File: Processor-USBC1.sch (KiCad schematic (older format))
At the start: 8 parts, among them J16 201267-0005, Q13 BSS138W, U28 PESD5V0X1BQ,115

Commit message: PVT
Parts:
- renumbered C104 to C99, Q13 to Q14, R77 to R68, R78 to R69, R79 to R70, R80 to R71, U28 to U26
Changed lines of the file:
@@
 encoding utf-8
 Sheet 11 24
-Title "Phoenix DVT"
-Date "2020-05-18"
+Title "Phoenix PVT"
+Date "2020-07-19"
 Rev "1"
 Comp ""
@@
 	7800 3500 7800 3400
 $Comp
-L supply-alias:GND #PWR0235
+L supply-alias:GND #PWR0223
 U 1 1 5E9C1E1F
 P 4600 2500
-F 0 "#PWR0235" H 4600 2250 50  0001 C CNN
+F 0 "#PWR0223" H 4600 2250 50  0001 C CNN
 F 1 "GND" H 4600 2350 50  0000 C CNN
 F 2 "" H 4600 2500 50  0001 C CNN
@@
 	6900 2900 6900 4100
 $Comp
-L supply-alias:GND #PWR0240
+L supply-alias:GND #PWR0228
 U 1 1 5EBF6DC2
 P 6900 4400
-F 0 "#PWR0240" H 6900 4150 50  0001 C CNN
+F 0 "#PWR0228" H 6900 4150 50  0001 C CNN
 F 1 "GND" H 6900 4250 50  0000 C CNN
 F 2 "" H 6900 4400 50  0001 C CNN
@@
 	6900 4400 6900 4300
 $Comp
-L supply-alias:GND #PWR0241
+L supply-alias:GND #PWR0229
 U 1 1 5E9C1E2B
 P 7100 4400
-F 0 "#PWR0241" H 7100 4150 50  0001 C CNN
+F 0 "#PWR0229" H 7100 4150 50  0001 C CNN
 F 1 "GND" H 7100 4250 50  0000 C CNN
 F 2 "" H 7100 4400 50  0001 C CNN
@@
 P 5100 1600
 AR Path="/5E9E174E/5E7A14E6/5E9C1E22" Ref="Q?"  Part="1"
-AR Path="/5E9E174E/5E76846F/5E9C1E22" Ref="Q13"  Part="1"
-F 0 "Q13" H 5300 1650 50  0000 L CNN
+AR Path="/5E9E174E/5E76846F/5E9C1E22" Ref="Q14"  Part="1"
+F 0 "Q14" H 5300 1650 50  0000 L CNN
 F 1 "BSS138W" H 5300 1550 50  0000 L CNN
 F 2 "IC-SOP:SC70-3" H 5300 1700 50  0001 C CNN
@@
 $EndComp
 $Comp
-L passive:C C104
+L passive:C C99
 U 1 1 5E9C1E30
 P 6100 1800
-F 0 "C104" H 6200 1850 50  0000 L CNN
+F 0 "C99" H 6200 1850 50  0000 L CNN
 F 1 "100n" H 6200 1750 50  0000 L CNN
 F 2 "Capacitor-Chip:C_CHIP_1005_Hand_NoSilk" H 6200 1700 50  0001 C CNN
@@
 $EndComp
 $Comp
-L passive:R R79
+L passive:R R70
 U 1 1 5E9C1E29
 P 6900 4200
-F 0 "R79" H 6950 4250 50  0000 L CNN
+F 0 "R70" H 6950 4250 50  0000 L CNN
 F 1 "5.1k" H 6950 4150 50  0000 L CNN
 F 2 "Resistor-Chip:R_CHIP_1005_Hand_NoSilk" V 6950 4100 50  0001 C CNN
@@
 $EndComp
 $Comp
-L passive:R R80
+L passive:R R71
 U 1 1 5E9C1E28
 P 7100 4200
-F 0 "R80" H 7150 4250 50  0000 L CNN
+F 0 "R71" H 7150 4250 50  0000 L CNN
 F 1 "5.1k" H 7150 4150 50  0000 L CNN
 F 2 "Resistor-Chip:R_CHIP_1005_Hand_NoSilk" V 7150 4100 50  0001 C CNN
@@
 USB_D+
 $Comp
-L supply-alias:GND #PWR0243
+L supply-alias:GND #PWR0231
 U 1 1 5E7D22C7
 P 8600 5300
-F 0 "#PWR0243" H 8600 5050 50  0001 C CNN
+F 0 "#PWR0231" H 8600 5050 50  0001 C CNN
 F 1 "GND" H 8600 5150 50  0000 C CNN
 F 2 "" H 8600 5300 50  0001 C CNN
@@
 $EndComp
 $Comp
-L supply-alias:GND #PWR0244
+L supply-alias:GND #PWR0232
 U 1 1 5E7D2BF8
 P 8900 5300
-F 0 "#PWR0244" H 8900 5050 50  0001 C CNN
+F 0 "#PWR0232" H 8900 5050 50  0001 C CNN
 F 1 "GND" H 8900 5150 50  0000 C CNN
 F 2 "" H 8900 5300 50  0001 C CNN
@@
 $EndComp
 $Comp
-L supply-alias:GND #PWR0239
+L supply-alias:GND #PWR0227
 U 1 1 5E9C1E2A
 P 6900 4400
-F 0 "#PWR0239" H 6900 4150 50  0001 C CNN
+F 0 "#PWR0227" H 6900 4150 50  0001 C CNN
 F 1 "GND" H 6900 4250 50  0000 C CNN
 F 2 "" H 6900 4400 50  0001 C CNN
@@
 $EndComp
 $Comp
-L supply-alias:GND #PWR0242
+L supply-alias:GND #PWR0230
 U 1 1 5EBF743C
 P 7100 4400
-F 0 "#PWR0242" H 7100 4150 50  0001 C CNN
+F 0 "#PWR0230" H 7100 4150 50  0001 C CNN
 F 1 "GND" H 7100 4250 50  0000 C CNN
 F 2 "" H 7100 4400 50  0001 C CNN
@@
 $EndComp
 $Comp
-L supply-alias:GND #PWR0238
+L supply-alias:GND #PWR0226
 U 1 1 5E9C1E31
 P 6100 1900
-F 0 "#PWR0238" H 6100 1650 50  0001 C CNN
+F 0 "#PWR0226" H 6100 1650 50  0001 C CNN
 F 1 "GND" H 6100 1750 50  0000 C CNN
 F 2 "" H 6100 1900 50  0001 C CNN
@@
 ~VBUS_DET
 $Comp
-L supply-alias:GND #PWR0236
+L supply-alias:GND #PWR0224
 U 1 1 5E9C1E24
 P 5000 1900
-F 0 "#PWR0236" H 5000 1650 50  0001 C CNN
+F 0 "#PWR0224" H 5000 1650 50  0001 C CNN
 F 1 "GND" H 5000 1750 50  0000 C CNN
 F 2 "" H 5000 1900 50  0001 C CNN
@@
 $EndComp
 $Comp
-L supply-alias:GND #PWR0237
+L supply-alias:GND #PWR0225
 U 1 1 5E9C1E26
 P 5400 1900
-F 0 "#PWR0237" H 5400 1650 50  0001 C CNN
+F 0 "#PWR0225" H 5400 1650 50  0001 C CNN
 F 1 "GND" H 5400 1750 50  0000 C CNN
 F 2 "" H 5400 1900 50  0001 C CNN
@@
 P 5400 1800
 AR Path="/5E9E174E/5E7A14E6/5E9C1E23" Ref="R?"  Part="1"
-AR Path="/5E9E174E/5E76846F/5E9C1E23" Ref="R77"  Part="1"
-F 0 "R77" H 5450 1850 50  0000 L CNN
+AR Path="/5E9E174E/5E76846F/5E9C1E23" Ref="R68"  Part="1"
+F 0 "R68" H 5450 1850 50  0000 L CNN
 F 1 "10k" H 5450 1750 50  0000 L CNN
 F 2 "Resistor-Chip:R_CHIP_1005_Hand_NoSilk" V 5450 1700 50  0001 C CNN
@@
 P 5000 2500
 AR Path="/5E9E174E/5EE65BF3/5E7D159C" Ref="U?"  Part="1"
-AR Path="/5E9E174E/5E76846F/5E7D159C" Ref="U28"  Part="1"
-F 0 "U28" H 5000 2750 50  0000 C CNN
+AR Path="/5E9E174E/5E76846F/5E7D159C" Ref="U26"  Part="1"
+F 0 "U26" H 5000 2750 50  0000 C CNN
 F 1 "PESD5V0X1BQ,115	" H 5000 2250 50  0000 C CNN
 F 2 "IC-SOT:SOT663" H 5000 2500 50  0001 C CNN
@@
 P 5700 1600
 AR Path="/5E9E174E/5E7A14E6/5EA4CED9" Ref="R?"  Part="1"
-AR Path="/5E9E174E/5E76846F/5EA4CED9" Ref="R78"  Part="1"
-F 0 "R78" V 5505 1600 50  0000 C CNN
+AR Path="/5E9E174E/5E76846F/5EA4CED9" Ref="R69"  Part="1"
+F 0 "R69" V 5505 1600 50  0000 C CNN
 F 1 "10k" V 5596 1600 50  0000 C CNN
 F 2 "Resistor-Chip:R_CHIP_1005_Hand_NoSilk" V 5750 1500 50  0001 C CNN

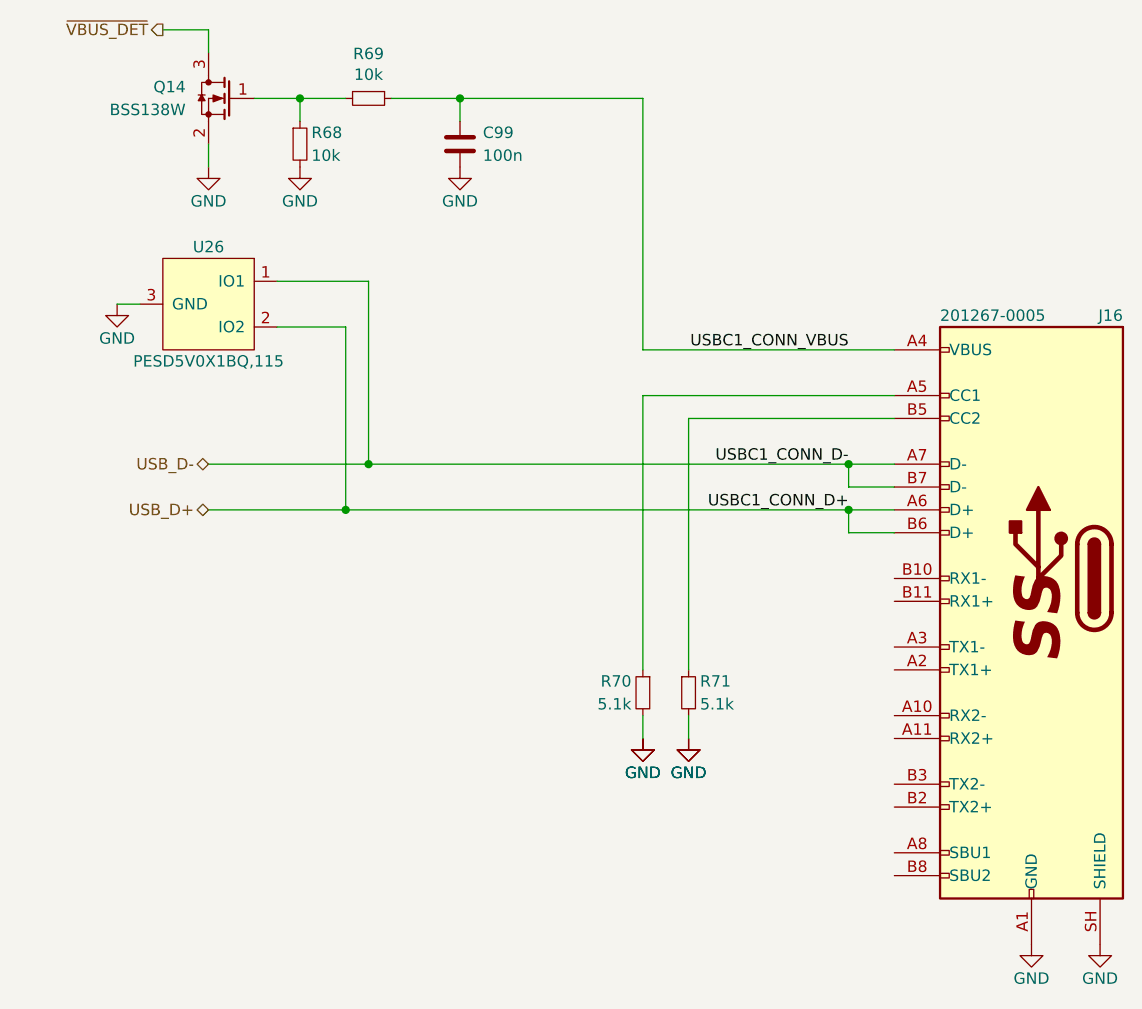
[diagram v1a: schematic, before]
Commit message: SBUにTVSダイオードを追加
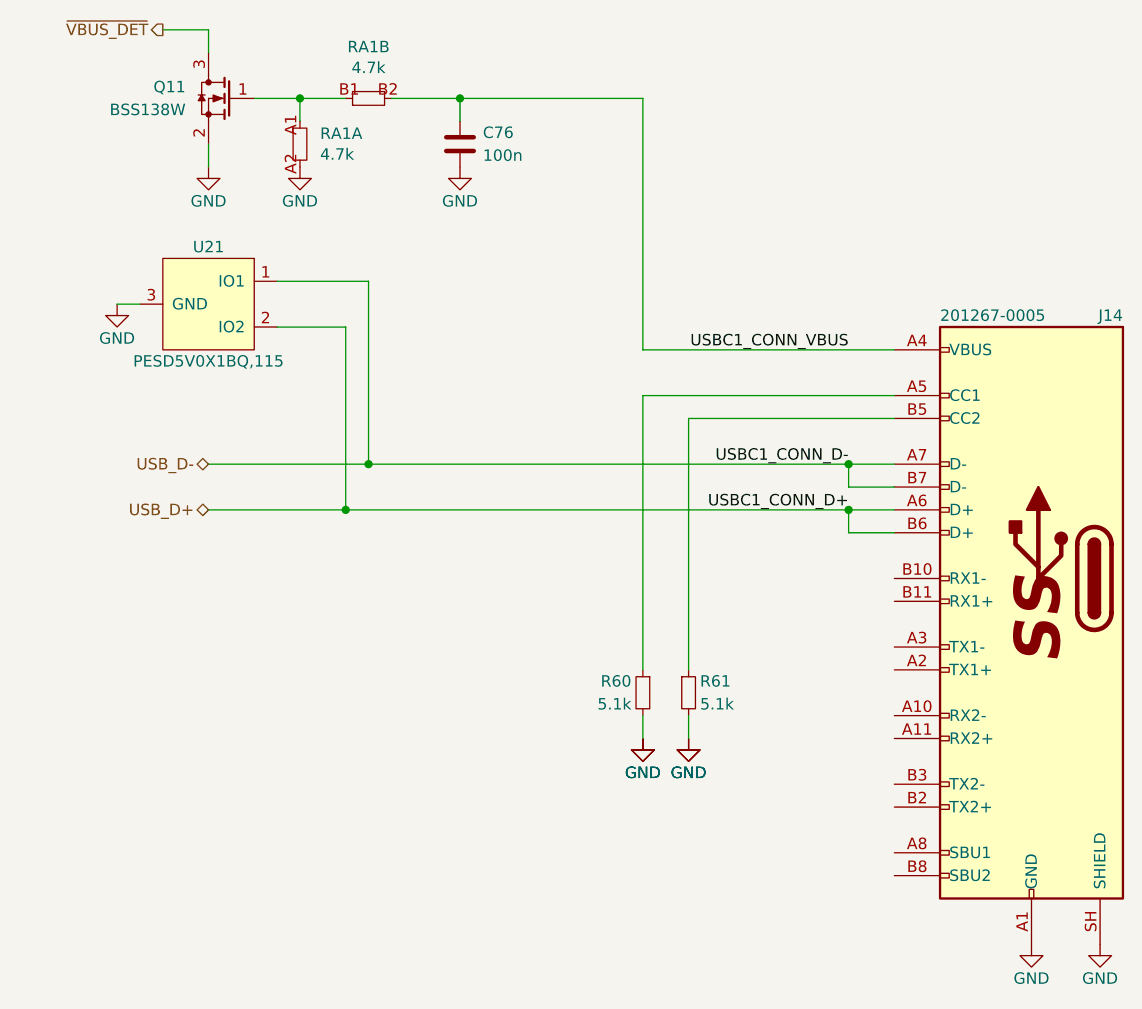
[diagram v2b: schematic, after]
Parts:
- removed R68, R69: 10k, Resistor-Chip:R_CHIP_1005_Hand_NoSilk, symbol passive:R
- added RA1: 4.7k, Resistor-Chip:R_CHIP_4x1005_CONCAVE, symbol passive:R_Array_4
- U21: renamed from U26; value PESD5V0X1BQ,115 -> PESD5V0X1BQ,115
- renumbered C99 to C76, J16 to J14, Q14 to Q11, R70 to R60, R71 to R61
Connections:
- net GND: now also RA1.A2
- net USBC1_CONN_VBUS: now also RA1.B2
- net at Q11.1 (G): now also RA1.A1, RA1.B1
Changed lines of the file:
@@
 $Descr A4 11693 8268
 encoding utf-8
-Sheet 11 24
+Sheet 10 24
 Title "Phoenix PVT"
 Date "2020-07-19"
@@
 	7800 3500 7800 3400
 $Comp
-L supply-alias:GND #PWR0223
+L supply-alias:GND #PWR0192
 U 1 1 5E9C1E1F
 P 4600 2500
-F 0 "#PWR0223" H 4600 2250 50  0001 C CNN
+F 0 "#PWR0192" H 4600 2250 50  0001 C CNN
 F 1 "GND" H 4600 2350 50  0000 C CNN
 F 2 "" H 4600 2500 50  0001 C CNN
@@
 	6900 2900 6900 4100
 $Comp
-L supply-alias:GND #PWR0228
+L supply-alias:GND #PWR0197
 U 1 1 5EBF6DC2
 P 6900 4400
-F 0 "#PWR0228" H 6900 4150 50  0001 C CNN
+F 0 "#PWR0197" H 6900 4150 50  0001 C CNN
 F 1 "GND" H 6900 4250 50  0000 C CNN
 F 2 "" H 6900 4400 50  0001 C CNN
@@
 	6900 4400 6900 4300
 $Comp
-L supply-alias:GND #PWR0229
+L supply-alias:GND #PWR0198
 U 1 1 5E9C1E2B
 P 7100 4400
-F 0 "#PWR0229" H 7100 4150 50  0001 C CNN
+F 0 "#PWR0198" H 7100 4150 50  0001 C CNN
 F 1 "GND" H 7100 4250 50  0000 C CNN
 F 2 "" H 7100 4400 50  0001 C CNN
@@
 P 5100 1600
 AR Path="/5E9E174E/5E7A14E6/5E9C1E22" Ref="Q?"  Part="1"
-AR Path="/5E9E174E/5E76846F/5E9C1E22" Ref="Q14"  Part="1"
-F 0 "Q14" H 5300 1650 50  0000 L CNN
+AR Path="/5E9E174E/5E76846F/5E9C1E22" Ref="Q11"  Part="1"
+F 0 "Q11" H 5300 1650 50  0000 L CNN
 F 1 "BSS138W" H 5300 1550 50  0000 L CNN
 F 2 "IC-SOP:SC70-3" H 5300 1700 50  0001 C CNN
@@
 $EndComp
 $Comp
-L passive:C C99
+L passive:C C76
 U 1 1 5E9C1E30
 P 6100 1800
-F 0 "C99" H 6200 1850 50  0000 L CNN
+F 0 "C76" H 6200 1850 50  0000 L CNN
 F 1 "100n" H 6200 1750 50  0000 L CNN
 F 2 "Capacitor-Chip:C_CHIP_1005_Hand_NoSilk" H 6200 1700 50  0001 C CNN
@@
 $EndComp
 $Comp
-L passive:R R70
+L passive:R R60
 U 1 1 5E9C1E29
 P 6900 4200
-F 0 "R70" H 6950 4250 50  0000 L CNN
+F 0 "R60" H 6950 4250 50  0000 L CNN
 F 1 "5.1k" H 6950 4150 50  0000 L CNN
 F 2 "Resistor-Chip:R_CHIP_1005_Hand_NoSilk" V 6950 4100 50  0001 C CNN
@@
 $EndComp
 $Comp
-L passive:R R71
+L passive:R R61
 U 1 1 5E9C1E28
 P 7100 4200
-F 0 "R71" H 7150 4250 50  0000 L CNN
+F 0 "R61" H 7150 4250 50  0000 L CNN
 F 1 "5.1k" H 7150 4150 50  0000 L CNN
 F 2 "Resistor-Chip:R_CHIP_1005_Hand_NoSilk" V 7150 4100 50  0001 C CNN
@@
 P 8600 3700
 AR Path="/5E76C88C" Ref="J?"  Part="1"
-AR Path="/5E9E174E/5E76846F/5E76C88C" Ref="J16"  Part="1"
-F 0 "J16" H 8200 4850 50  0000 L CNN
+AR Path="/5E9E174E/5E76846F/5E76C88C" Ref="J14"  Part="1"
+F 0 "J14" H 8200 4850 50  0000 L CNN
 F 1 "201267-0005" H 9000 4850 50  0000 R CNN
 F 2 "Connector-Molex:2012670005" H 8750 3700 50  0001 C CNN
@@
 USB_D+
 $Comp
-L supply-alias:GND #PWR0231
+L supply-alias:GND #PWR0200
 U 1 1 5E7D22C7
 P 8600 5300
-F 0 "#PWR0231" H 8600 5050 50  0001 C CNN
+F 0 "#PWR0200" H 8600 5050 50  0001 C CNN
 F 1 "GND" H 8600 5150 50  0000 C CNN
 F 2 "" H 8600 5300 50  0001 C CNN
@@
 $EndComp
 $Comp
-L supply-alias:GND #PWR0232
+L supply-alias:GND #PWR0201
 U 1 1 5E7D2BF8
 P 8900 5300
-F 0 "#PWR0232" H 8900 5050 50  0001 C CNN
+F 0 "#PWR0201" H 8900 5050 50  0001 C CNN
 F 1 "GND" H 8900 5150 50  0000 C CNN
 F 2 "" H 8900 5300 50  0001 C CNN
@@
 $EndComp
 $Comp
-L supply-alias:GND #PWR0227
+L supply-alias:GND #PWR0196
 U 1 1 5E9C1E2A
 P 6900 4400
-F 0 "#PWR0227" H 6900 4150 50  0001 C CNN
+F 0 "#PWR0196" H 6900 4150 50  0001 C CNN
 F 1 "GND" H 6900 4250 50  0000 C CNN
 F 2 "" H 6900 4400 50  0001 C CNN
@@
 $EndComp
 $Comp
-L supply-alias:GND #PWR0230
+L supply-alias:GND #PWR0199
 U 1 1 5EBF743C
 P 7100 4400
-F 0 "#PWR0230" H 7100 4150 50  0001 C CNN
+F 0 "#PWR0199" H 7100 4150 50  0001 C CNN
 F 1 "GND" H 7100 4250 50  0000 C CNN
 F 2 "" H 7100 4400 50  0001 C CNN
@@
 $EndComp
 $Comp
-L supply-alias:GND #PWR0226
+L supply-alias:GND #PWR0195
 U 1 1 5E9C1E31
 P 6100 1900
-F 0 "#PWR0226" H 6100 1650 50  0001 C CNN
+F 0 "#PWR0195" H 6100 1650 50  0001 C CNN
 F 1 "GND" H 6100 1750 50  0000 C CNN
 F 2 "" H 6100 1900 50  0001 C CNN
@@
 ~VBUS_DET
 $Comp
-L supply-alias:GND #PWR0224
+L supply-alias:GND #PWR0193
 U 1 1 5E9C1E24
 P 5000 1900
-F 0 "#PWR0224" H 5000 1650 50  0001 C CNN
+F 0 "#PWR0193" H 5000 1650 50  0001 C CNN
 F 1 "GND" H 5000 1750 50  0000 C CNN
 F 2 "" H 5000 1900 50  0001 C CNN
@@
 $EndComp
 $Comp
-L supply-alias:GND #PWR0225
+L supply-alias:GND #PWR0194
 U 1 1 5E9C1E26
 P 5400 1900
-F 0 "#PWR0225" H 5400 1650 50  0001 C CNN
+F 0 "#PWR0194" H 5400 1650 50  0001 C CNN
 F 1 "GND" H 5400 1750 50  0000 C CNN
 F 2 "" H 5400 1900 50  0001 C CNN
@@
 $EndComp
 $Comp
-L passive:R R?
-U 1 1 5E9C1E23
-P 5400 1800
-AR Path="/5E9E174E/5E7A14E6/5E9C1E23" Ref="R?"  Part="1"
-AR Path="/5E9E174E/5E76846F/5E9C1E23" Ref="R68"  Part="1"
-F 0 "R68" H 5450 1850 50  0000 L CNN
-F 1 "10k" H 5450 1750 50  0000 L CNN
-F 2 "Resistor-Chip:R_CHIP_1005_Hand_NoSilk" V 5450 1700 50  0001 C CNN
-F 3 "" H 5450 1900 50  0001 C CNN
-F 4 "RK73H1ETTP1002F" H 5400 1800 50  0001 C CNN "PartName"
-F 5 "P板" H 5400 1800 50  0001 C CNN "Supplier"
-	1    5400 1800
-	1    0    0    -1
-$EndComp
-$Comp
 L protection:TVS_2CH_1_2_GND3 U?
 U 1 1 5E7D159C
 P 5000 2500
 AR Path="/5E9E174E/5EE65BF3/5E7D159C" Ref="U?"  Part="1"
-AR Path="/5E9E174E/5E76846F/5E7D159C" Ref="U26"  Part="1"
-F 0 "U26" H 5000 2750 50  0000 C CNN
-F 1 "PESD5V0X1BQ,115	" H 5000 2250 50  0000 C CNN
+AR Path="/5E9E174E/5E76846F/5E7D159C" Ref="U21"  Part="1"
+F 0 "U21" H 5000 2750 50  0000 C CNN
+F 1 "PESD5V0X1BQ,115" H 5000 2250 50  0000 C CNN
 F 2 "IC-SOT:SOT663" H 5000 2500 50  0001 C CNN
 F 3 "" H 5000 2500 50  0001 C CNN
@@
 Connection ~ 7800 3400
 Connection ~ 5600 3400
-$Comp
-L passive:R R?
-U 1 1 5EA4CED9
+Wire Wire Line
+	5800 1600 6100 1600
+Wire Wire Line
+	6100 1600 6900 1600
+$Comp
+L passive:R_Array_4 RA?
+U 1 1 5F334588
+P 5400 1800
+AR Path="/5E4B5B3E/5F334588" Ref="RA?"  Part="2"
+AR Path="/5E4B5786/5F334588" Ref="RA?"  Part="2"
+AR Path="/5F235278/5F334588" Ref="RA?"  Part="3"
+AR Path="/5F235A43/5F334588" Ref="RA?"  Part="3"
+AR Path="/5E9E174E/5F334588" Ref="RA?"  Part="2"
+AR Path="/5E9E174E/5E76846F/5F334588" Ref="RA1"  Part="1"
+F 0 "RA1" H 5488 1846 50  0000 L CNN
+F 1 "4.7k" H 5488 1755 50  0000 L CNN
+F 2 "Resistor-Chip:R_CHIP_4x1005_CONCAVE" H 5400 1800 50  0001 C CNN
+F 3 "" H 5400 1800 50  0001 C CNN
+F 4 "EXB-N8V472JX" H 5400 1800 50  0001 C CNN "PartName"
+	1    5400 1800
+	1    0    0    -1
+$EndComp
+$Comp
+L passive:R_Array_4 RA?
+U 2 1 5F334A92
 P 5700 1600
-AR Path="/5E9E174E/5E7A14E6/5EA4CED9" Ref="R?"  Part="1"
-AR Path="/5E9E174E/5E76846F/5EA4CED9" Ref="R69"  Part="1"
-F 0 "R69" V 5505 1600 50  0000 C CNN
-F 1 "10k" V 5596 1600 50  0000 C CNN
-F 2 "Resistor-Chip:R_CHIP_1005_Hand_NoSilk" V 5750 1500 50  0001 C CNN
-F 3 "" H 5750 1700 50  0001 C CNN
-F 4 "RK73H1ETTP1002F" H 5700 1600 50  0001 C CNN "PartName"
-F 5 "P板" H 5700 1600 50  0001 C CNN "Supplier"
-	1    5700 1600
-	0    1    1    0
-$EndComp
-Wire Wire Line
-	5800 1600 6100 1600
-Wire Wire Line
-	6100 1600 6900 1600
+AR Path="/5E4B5B3E/5F334A92" Ref="RA?"  Part="2"
+AR Path="/5E4B5786/5F334A92" Ref="RA?"  Part="2"
+AR Path="/5F235278/5F334A92" Ref="RA?"  Part="3"
+AR Path="/5F235A43/5F334A92" Ref="RA?"  Part="3"
+AR Path="/5E9E174E/5F334A92" Ref="RA?"  Part="2"
+AR Path="/5E9E174E/5E76846F/5F334A92" Ref="RA1"  Part="2"
+F 0 "RA1" V 5925 1600 50  0000 C CNN
+F 1 "4.7k" V 5834 1600 50  0000 C CNN
+F 2 "Resistor-Chip:R_CHIP_4x1005_CONCAVE" H 5700 1600 50  0001 C CNN
+F 3 "" H 5700 1600 50  0001 C CNN
+F 4 "EXB-N8V472JX" H 5700 1600 50  0001 C CNN "PartName"
+	2    5700 1600
+	0    -1   -1   0
+$EndComp
 $EndSCHEMATC
